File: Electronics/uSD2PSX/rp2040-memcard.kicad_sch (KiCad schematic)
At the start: 40 parts, among them J101 PS2, J102 BSEL, J103 GND, J104 3V3, J105 SCL, J106 SDA, J107 SWC, J108 SWD, J110 DP, J111 DN, J112 GND, J113 3V3, J114 MEM2085-00-115-00-A_REV0.2, U101 W25Q16JVUXIQ, U102 RP2040, U4 LY68L6400SLIT, Y101 12MHz

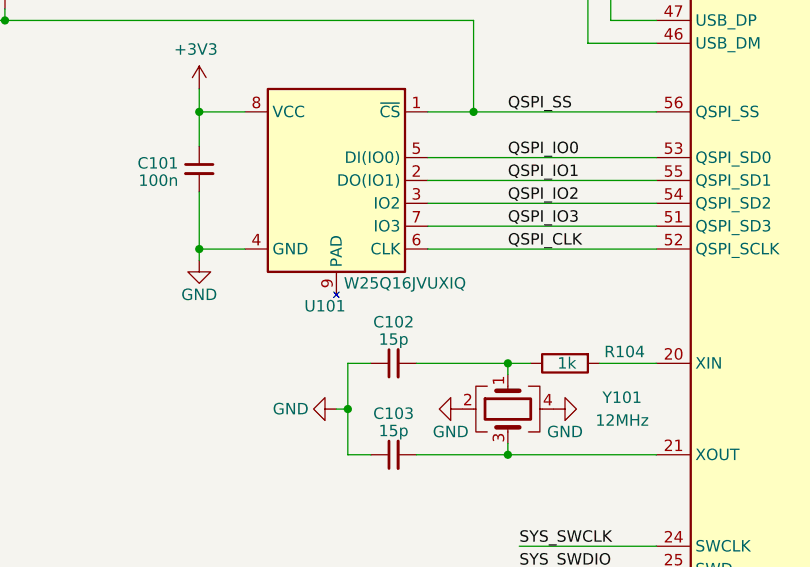
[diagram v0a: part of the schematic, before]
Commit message: correct part number of uSD2PSX SPI flash
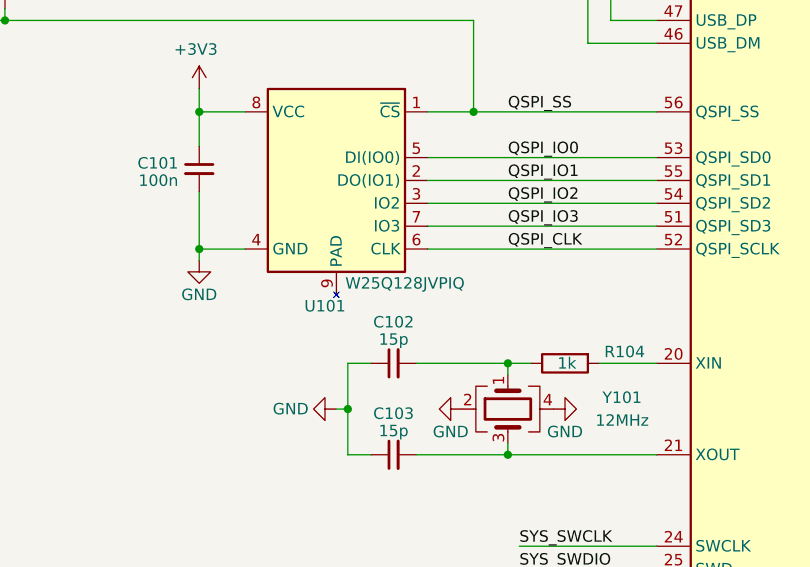
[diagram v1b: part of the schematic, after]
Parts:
- U101: value W25Q16JVUXIQ -> W25Q128JVPIQ; Part Number W25Q16JVUXIQ TR -> W25Q128JVPIQ
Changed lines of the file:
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@@
       (effects (font (size 1.27 1.27)))
     )
-    (property "Value" "W25Q16JVUXIQ" (at 96.52 95.25 0)
+    (property "Value" "W25Q128JVPIQ" (at 96.52 95.25 0)
       (effects (font (size 1.27 1.27)))
     )
@@
       (effects (font (size 1.27 1.27)) hide)
     )
-    (property "Datasheet" "https://www.winbond.com/resource-files/w25q16jv%20spi%20revh%2004082019%20plus.pdf" (at 88.9 83.82 0)
+    (property "Datasheet" "https://www.winbond.com/resource-files/w25q128jv%20revf%2003272018%20plus.pdf" (at 88.9 83.82 0)
       (effects (font (size 1.27 1.27)) hide)
     )
-    (property "Part Number" "W25Q16JVUXIQ TR" (at 88.9 83.82 0)
+    (property "Part Number" "W25Q128JVPIQ" (at 88.9 83.82 0)
       (effects (font (size 1.27 1.27)) hide)
     )
